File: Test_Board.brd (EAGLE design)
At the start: 63.5 x 57.1 mm, 33 parts, among them U1 Value, U2 Value

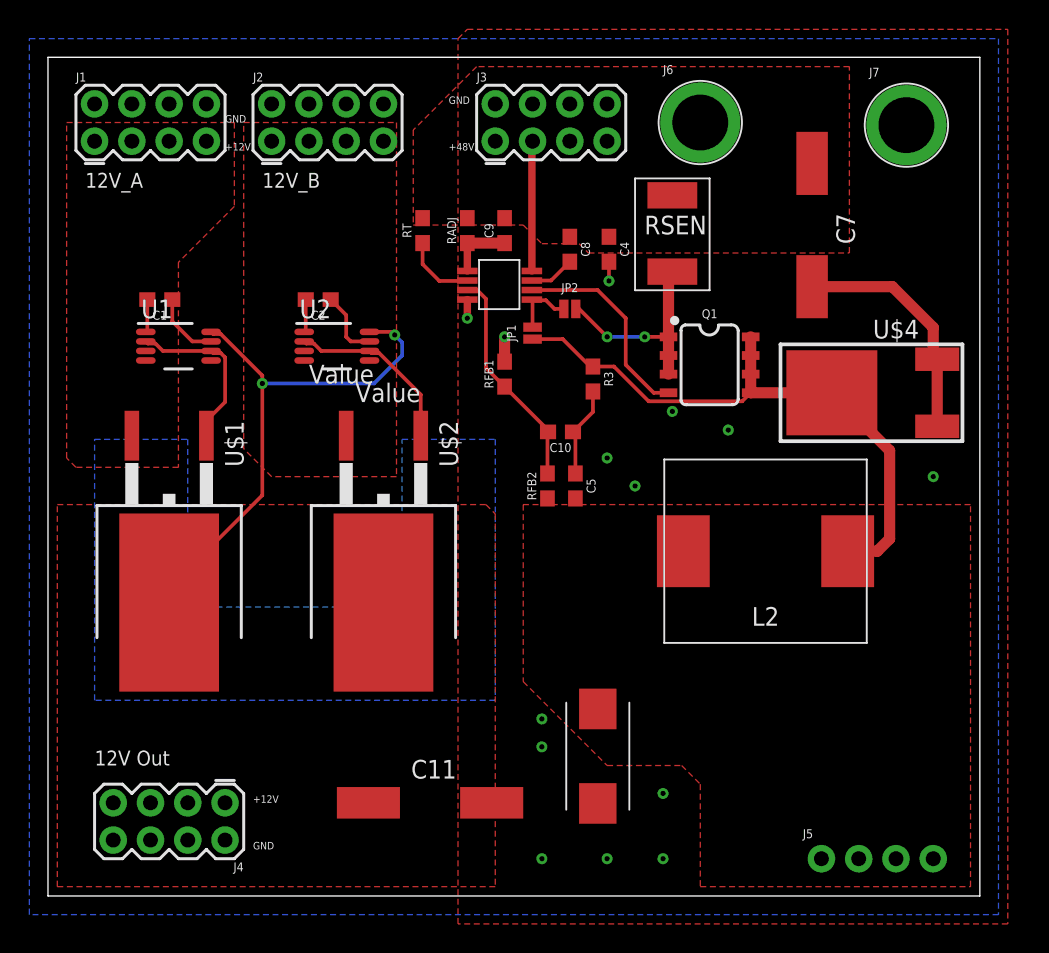
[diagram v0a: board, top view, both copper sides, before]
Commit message: bigger U and a few labels. inductor pour cutout
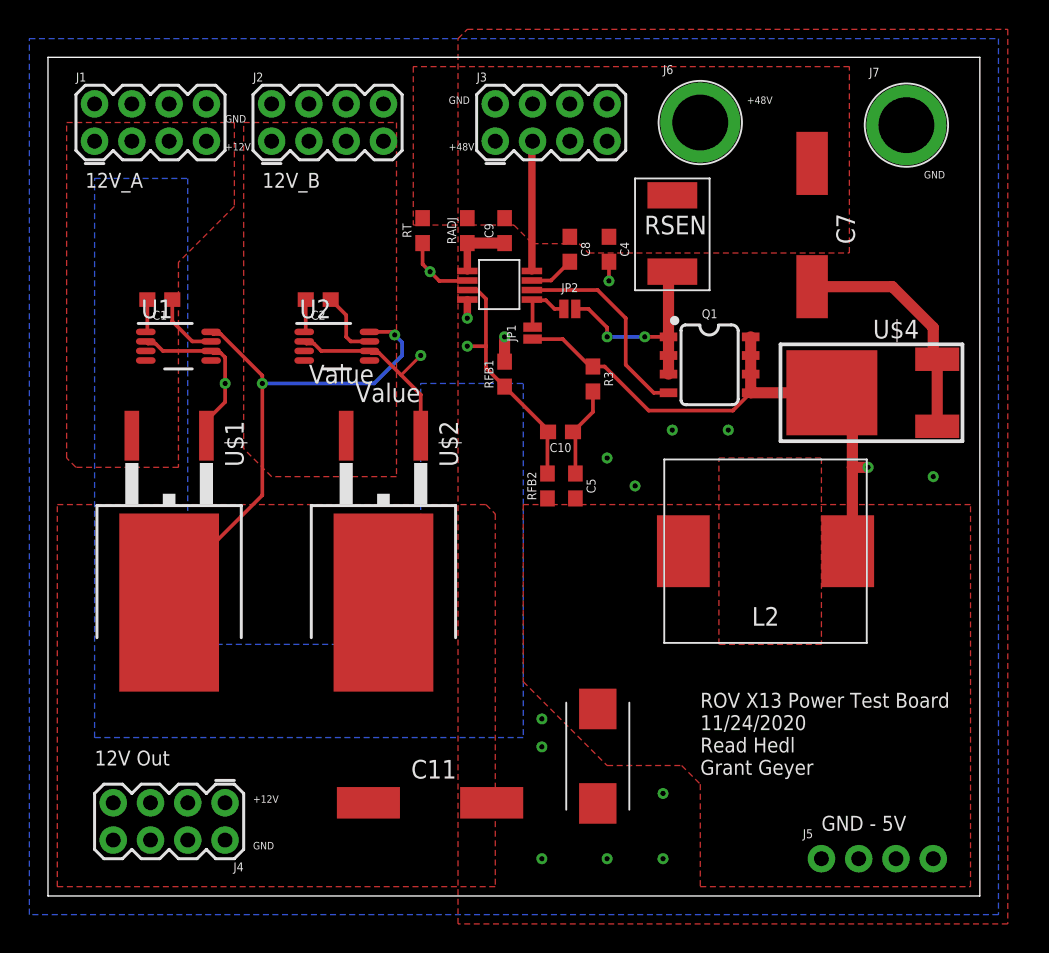
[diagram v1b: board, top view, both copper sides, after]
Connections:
- net N$11 renamed SW
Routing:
- net N$13: track 12.2 -> 14.1 mm, vias 0 -> 1
- net SW: track 41.0 -> 39.5 mm, vias 0 -> 1
- net FB: track 15.2 -> 16.5 mm, vias 0 -> 1
- net RT: vias 0 -> 1
- net N$10: vias 0 -> 1
- added copper zone on layer 1, net X
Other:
- board text added: "GND - 5V"
- board text added: "ROV X13 Power Test Board 11/24/2020 Read Hedl Grant Geyer"
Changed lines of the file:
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@@
 <?xml version="1.0" encoding="utf-8"?>
 <!DOCTYPE eagle SYSTEM "eagle.dtd">
-<eagle version="9.5.0">
+<eagle version="9.6.0">
 <drawing>
 <settings>
@@
 <text x="1.27" y="3.175" size="0.508" layer="21">GND</text>
 <polygon width="0.381" layer="30">
-<vertex x="-9.525" y="13.335"/>
-<vertex x="-9.525" y="31.115"/>
-<vertex x="-3.175" y="31.115"/>
-<vertex x="-3.175" y="19.685"/>
-<vertex x="11.43" y="19.685"/>
-<vertex x="11.43" y="31.115"/>
-<vertex x="17.78" y="31.115"/>
-<vertex x="17.78" y="13.335"/>
+<vertex x="-9.525" y="10.795"/>
+<vertex x="-9.525" y="48.895"/>
+<vertex x="-3.175" y="48.895"/>
+<vertex x="-3.175" y="17.145"/>
+<vertex x="12.7" y="17.145"/>
+<vertex x="12.7" y="34.925"/>
+<vertex x="19.685" y="34.925"/>
+<vertex x="19.685" y="10.795"/>
 </polygon>
+<text x="31.75" y="8.255" size="1.016" layer="25">ROV X13 Power Test Board
+11/24/2020
+Read Hedl
+Grant Geyer</text>
+<text x="40.005" y="4.445" size="1.016" layer="25">GND - 5V</text>
+<text x="34.925" y="53.975" size="0.508" layer="21">+48V</text>
+<text x="46.99" y="48.895" size="0.508" layer="21">GND</text>
 </plain>
 <attributes>
@@
 <wire x1="-5.37606875" y1="37.6444" x2="-4.87166875" y2="37.14" width="0.254" layer="1"/>
 <wire x1="-0.92606875" y1="36.99439375" x2="-0.6306" y2="36.698925" width="0.254" layer="1"/>
-<wire x1="-1.584996875" y1="37.14" x2="-1.439390625" y2="36.99439375" width="0.254" layer="1"/>
+<wire x1="-1.439390625" y1="36.99439375" x2="-1.584996875" y2="37.14" width="0.254" layer="1"/>
 <wire x1="-1.439390625" y1="36.99439375" x2="-0.92606875" y2="36.99439375" width="0.254" layer="1"/>
-<wire x1="-0.6306" y1="36.698925" x2="-0.6306" y2="33.6594" width="0.254" layer="1"/>
+<wire x1="-0.6306" y1="36.698925" x2="-0.6306" y2="34.925" width="0.254" layer="1"/>
+<wire x1="-0.6306" y1="33.6594" x2="-0.6306" y2="34.925" width="0.254" layer="1"/>
 <wire x1="-1.905" y1="32.385" x2="-0.6306" y2="33.6594" width="0.254" layer="1"/>
 <wire x1="-1.905" y1="31.365" x2="-1.905" y2="32.385" width="0.254" layer="1"/>
+<via x="-0.6306" y="34.925" extent="1-16" drill="0.35"/>
 </signal>
 <signal name="N$13">
@@
 <wire x1="9.210003125" y1="37.14" x2="9.355609375" y2="36.99439375" width="0.254" layer="1"/>
 <wire x1="9.355609375" y1="36.99439375" x2="9.86893125" y2="36.99439375" width="0.254" layer="1"/>
-<wire x1="9.86893125" y1="36.99439375" x2="12.7" y2="34.163325" width="0.254" layer="1"/>
-<wire x1="12.7" y1="34.163325" x2="12.7" y2="33.02" width="0.254" layer="1"/>
-<wire x1="12.7" y1="33.02" x2="12.7" y2="32.385" width="0.254" layer="1"/>
-<wire x1="12.7" y1="31.365" x2="12.7" y2="32.385" width="0.254" layer="1"/>
+<wire x1="9.86893125" y1="36.99439375" x2="11.3666625" y2="35.4966625" width="0.254" layer="1"/>
+<wire x1="11.3666625" y1="35.4966625" x2="12.3191625" y2="34.5441625" width="0.254" layer="1"/>
+<wire x1="12.3191625" y1="34.5441625" x2="12.7" y2="34.163325" width="0.254" layer="1"/>
+<wire x1="12.7" y1="31.365" x2="12.7" y2="34.163325" width="0.254" layer="1"/>
+<wire x1="11.3666625" y1="35.4966625" x2="12.7" y2="36.83" width="0.2032" layer="1"/>
+<via x="12.7" y="36.83" extent="1-16" drill="0.35"/>
 </signal>
 <signal name="GND">
@@
 <via x="27.305" y="27.94" extent="1-16" drill="0.35"/>
 <via x="33.655" y="31.75" extent="1-16" drill="0.35"/>
-<via x="29.845" y="33.02" extent="1-16" drill="0.35"/>
+<via x="29.845" y="31.75" extent="1-16" drill="0.35"/>
 <via x="25.4" y="2.54" extent="1-16" drill="0.35"/>
 <via x="29.21" y="6.985" extent="1-16" drill="0.35"/>
@@
 <polygon width="0.508" layer="1">
 <vertex x="12.192" y="45.72"/>
-<vertex x="19.685" y="45.72"/>
-<vertex x="20.955" y="44.45"/>
+<vertex x="19.05" y="45.72"/>
+<vertex x="20.32" y="44.45"/>
 <vertex x="23.495" y="44.45"/>
 <vertex x="24.13" y="43.815"/>
 <vertex x="41.91" y="43.815"/>
 <vertex x="41.91" y="56.515"/>
-<vertex x="16.51" y="56.515"/>
-<vertex x="12.192" y="52.197"/>
+<vertex x="12.192" y="56.515"/>
 </polygon>
 <wire x1="20.275" y1="42.59" x2="20.275" y2="51.39" width="0.508" layer="1"/>
@@
 <wire x1="24.75" y1="41.29" x2="26.67" y2="39.37" width="0.254" layer="1"/>
 </signal>
-<signal name="N$11">
+<signal name="SW">
 <contactref element="Q1" pad="5"/>
 <contactref element="Q1" pad="6"/>
@@
 <wire x1="35.185" y1="36.83" x2="35.185" y2="35.56" width="0.762" layer="1"/>
 <wire x1="35.185" y1="35.56" x2="35.185" y2="34.29" width="0.762" layer="1"/>
-<wire x1="24.4348" y1="36.0798" x2="25.86506875" y2="36.0798" width="0.254" layer="1"/>
-<wire x1="25.86506875" y1="36.0798" x2="28.23426875" y2="33.7106" width="0.254" layer="1"/>
-<wire x1="34.6056" y1="33.7106" x2="28.23426875" y2="33.7106" width="0.254" layer="1"/>
-<wire x1="34.6056" y1="33.7106" x2="35.185" y2="34.29" width="0.254" layer="1"/>
-<wire x1="40.715" y1="34.29" x2="44.6532" y2="30.3518" width="0.762" layer="1"/>
-<wire x1="44.6532" y1="30.3518" x2="44.6532" y2="24.3332" width="0.762" layer="1"/>
-<wire x1="43.815" y1="23.495" x2="41.795" y2="23.495" width="0.762" layer="1"/>
-<wire x1="44.6532" y1="24.3332" x2="43.815" y2="23.495" width="0.762" layer="1"/>
+<wire x1="24.4348" y1="36.0798" x2="25.23006875" y2="36.0798" width="0.254" layer="1"/>
+<wire x1="25.23006875" y1="36.0798" x2="28.23426875" y2="33.0756" width="0.254" layer="1"/>
+<wire x1="33.9706" y1="33.0756" x2="28.23426875" y2="33.0756" width="0.254" layer="1"/>
+<wire x1="33.9706" y1="33.0756" x2="35.185" y2="34.29" width="0.254" layer="1"/>
+<wire x1="40.715" y1="34.29" x2="42.1132" y2="32.8918" width="0.762" layer="1"/>
+<wire x1="42.1132" y1="32.8918" x2="42.1132" y2="29.21" width="0.762" layer="1"/>
+<wire x1="42.1132" y1="23.495" x2="42.1132" y2="29.21" width="0.762" layer="1"/>
+<wire x1="42.1132" y1="23.495" x2="41.795" y2="23.495" width="0.762" layer="1"/>
 <wire x1="40.715" y1="34.29" x2="35.185" y2="34.29" width="0.762" layer="1"/>
+<wire x1="42.1132" y1="29.21" x2="43.18" y2="29.21" width="0.762" layer="1"/>
+<via x="43.18" y="29.21" extent="1-16" drill="0.35"/>
 </signal>
 <signal name="N$12">
@@
 <contactref element="RT" pad="1"/>
 <contactref element="U$3" pad="2"/>
-<wire x1="12.827" y1="43.053" x2="13.97" y2="41.91" width="0.254" layer="1"/>
+<wire x1="12.827" y1="43.053" x2="13.335" y2="42.545" width="0.254" layer="1"/>
+<wire x1="13.335" y1="42.545" x2="13.97" y2="41.91" width="0.254" layer="1"/>
 <wire x1="12.827" y1="43.053" x2="12.827" y2="44.489" width="0.254" layer="1"/>
 <wire x1="13.97" y1="41.91" x2="15.845" y2="41.91" width="0.254" layer="1"/>
 <wire x1="15.845" y1="41.91" x2="15.875" y2="41.94" width="0.254" layer="1"/>
+<via x="13.335" y="42.545" extent="1-16" drill="0.35"/>
 </signal>
 <signal name="FB">
@@
 <wire x1="21.375" y1="31.75" x2="18.415" y2="34.71" width="0.254" layer="1"/>
 <wire x1="18.415" y1="34.71" x2="17.145" y2="35.98" width="0.254" layer="1"/>
-<wire x1="17.145" y1="35.98" x2="17.145" y2="40.69013125" width="0.254" layer="1"/>
+<wire x1="17.145" y1="35.98" x2="17.145" y2="37.465" width="0.254" layer="1"/>
+<wire x1="17.145" y1="37.465" x2="17.145" y2="40.69013125" width="0.254" layer="1"/>
 <wire x1="16.54513125" y1="41.29" x2="17.145" y2="40.69013125" width="0.254" layer="1"/>
 <wire x1="15.875" y1="41.29" x2="16.54513125" y2="41.29" width="0.254" layer="1"/>
+<wire x1="17.145" y1="37.465" x2="15.875" y2="37.465" width="0.254" layer="1"/>
+<via x="15.875" y="37.465" extent="1-16" drill="0.35"/>
 </signal>
 <signal name="ISEN">
@@
 <wire x1="29.585" y1="38.1" x2="29.585" y2="36.83" width="0.762" layer="1"/>
 <wire x1="29.585" y1="36.83" x2="29.585" y2="35.56" width="0.762" layer="1"/>
-<wire x1="23.2664" y1="40.005" x2="23.495" y2="40.005" width="0.254" layer="1"/>
-<wire x1="23.495" y1="40.005" x2="25.4" y2="38.1" width="0.254" layer="1"/>
+<wire x1="23.2664" y1="40.005" x2="24.13" y2="40.005" width="0.254" layer="1"/>
+<wire x1="25.4" y1="38.735" x2="24.13" y2="40.005" width="0.254" layer="1"/>
+<wire x1="25.4" y1="38.735" x2="25.4" y2="38.1" width="0.254" layer="1"/>
 <via x="25.4" y="38.1" extent="1-16" drill="0.35"/>
 <wire x1="29.585" y1="38.1" x2="27.9626" y2="38.1" width="0.254" layer="1"/>
@@
 <signal name="TEST">
 <polygon width="0.381" layer="16">
-<vertex x="-9.525" y="13.335"/>
-<vertex x="-9.525" y="31.115"/>
-<vertex x="-3.175" y="31.115"/>
-<vertex x="-3.175" y="19.685"/>
-<vertex x="11.43" y="19.685"/>
-<vertex x="11.43" y="31.115"/>
-<vertex x="17.78" y="31.115"/>
-<vertex x="17.78" y="13.335"/>
+<vertex x="-9.525" y="10.795"/>
+<vertex x="-9.525" y="48.895"/>
+<vertex x="-3.175" y="48.895"/>
+<vertex x="-3.175" y="17.145"/>
+<vertex x="12.7" y="17.145"/>
+<vertex x="12.7" y="34.925"/>
+<vertex x="19.685" y="34.925"/>
+<vertex x="19.685" y="10.795"/>
+</polygon>
+</signal>
+<signal name="X">
+<polygon width="0.1524" layer="1" pour="cutout">
+<vertex x="33.02" y="29.845"/>
+<vertex x="40.005" y="29.845"/>
+<vertex x="40.005" y="17.145"/>
+<vertex x="33.02" y="17.145"/>
 </polygon>
 </signal>
@@
 </drawing>
 <compatibility>
+<note version="6.3" minversion="6.2.2" severity="warning">
+Since Version 6.2.2 text objects can contain more than one line,
+which will not be processed correctly with this version.
+</note>
 <note version="8.2" severity="warning">
 Since Version 8.2, EAGLE supports online libraries. The ids

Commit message: couple silkscreen changes to order
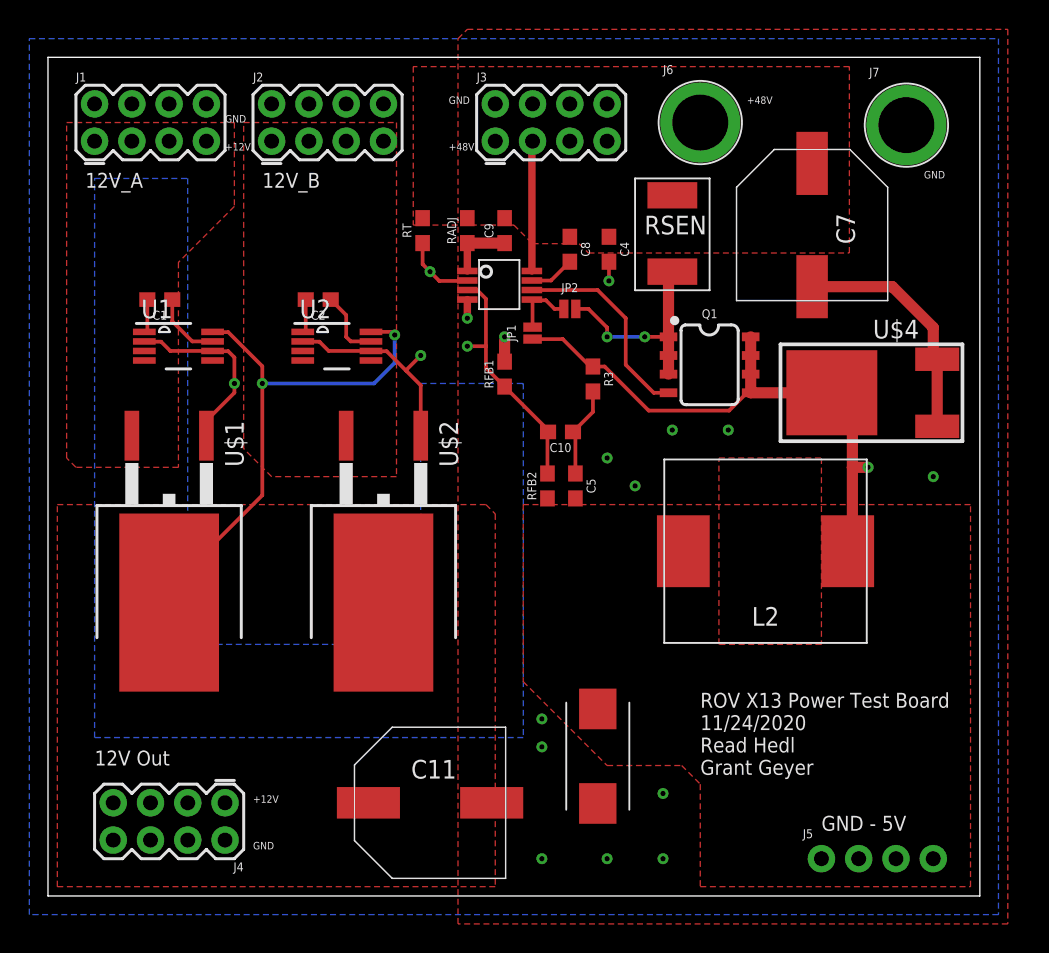
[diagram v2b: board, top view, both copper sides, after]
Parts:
- C7: value 47uF -> 330uF
- U1, U2: device Dist_OR_Controller:DGK0008A_N -> Dist_OR_Controller:DGK0008A_M
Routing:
- net N$10: track 11.7 -> 12.7 mm
